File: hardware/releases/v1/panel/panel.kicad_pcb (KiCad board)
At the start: 4 copper layers, 55.6 x 77.4 mm, 83 parts, among them J1 KF142R-5.08-2P, J101 FPC-05F-8PH20, J102 OLED, J2 2086-1204/700-000/997-605, J3 FPC-05F-8PH20, J4 KF142R-5.08-3P, J5 2086-1203/700-000/997-605, J6 2086-1203/700-000/997-605, K1 G6B-2114P-US DC5, Q1 MMBT3904, SW101 B3U-1000P, SW102 B3U-1000P, U1 SCT2601TVBR, U101 74AHCT1G125, U2 LM66100, U3 XIAO ESP32C6

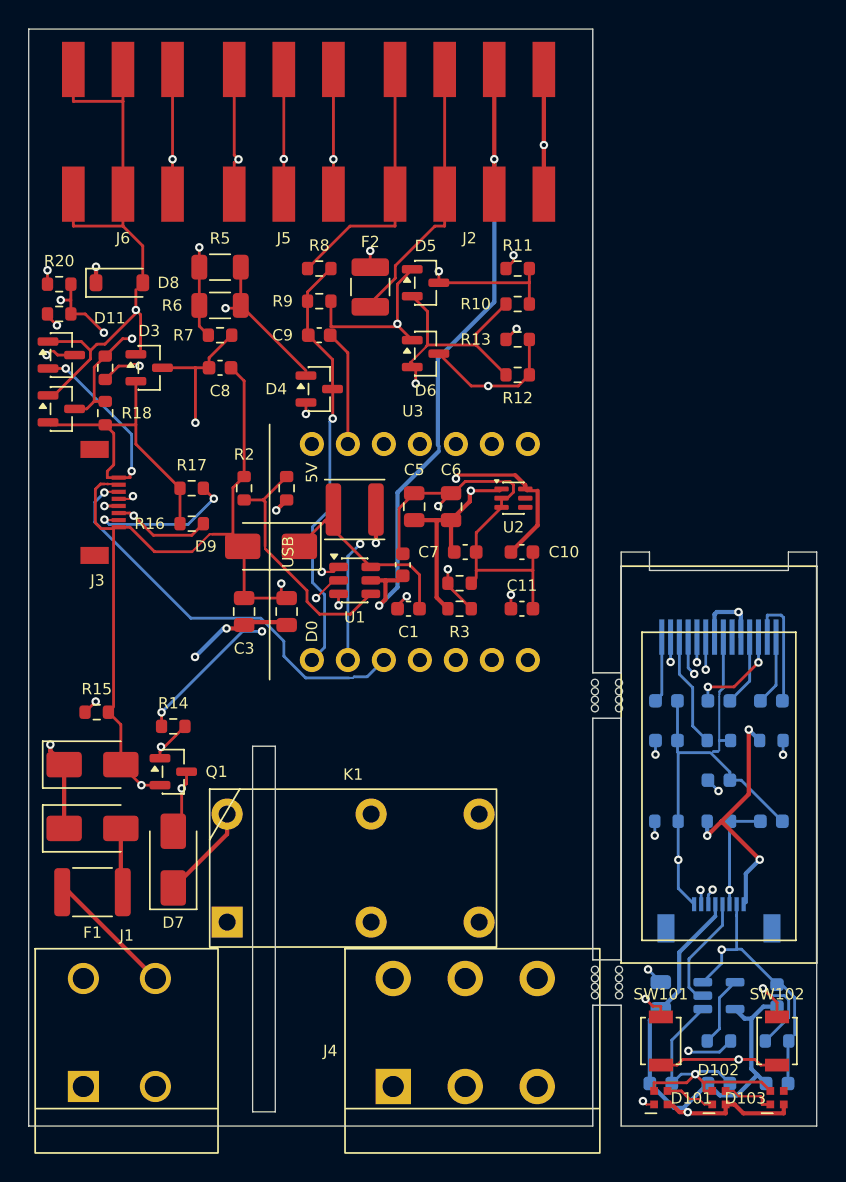
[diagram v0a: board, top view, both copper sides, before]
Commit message: extend GND track joints on main board to fully seat on pads/vias
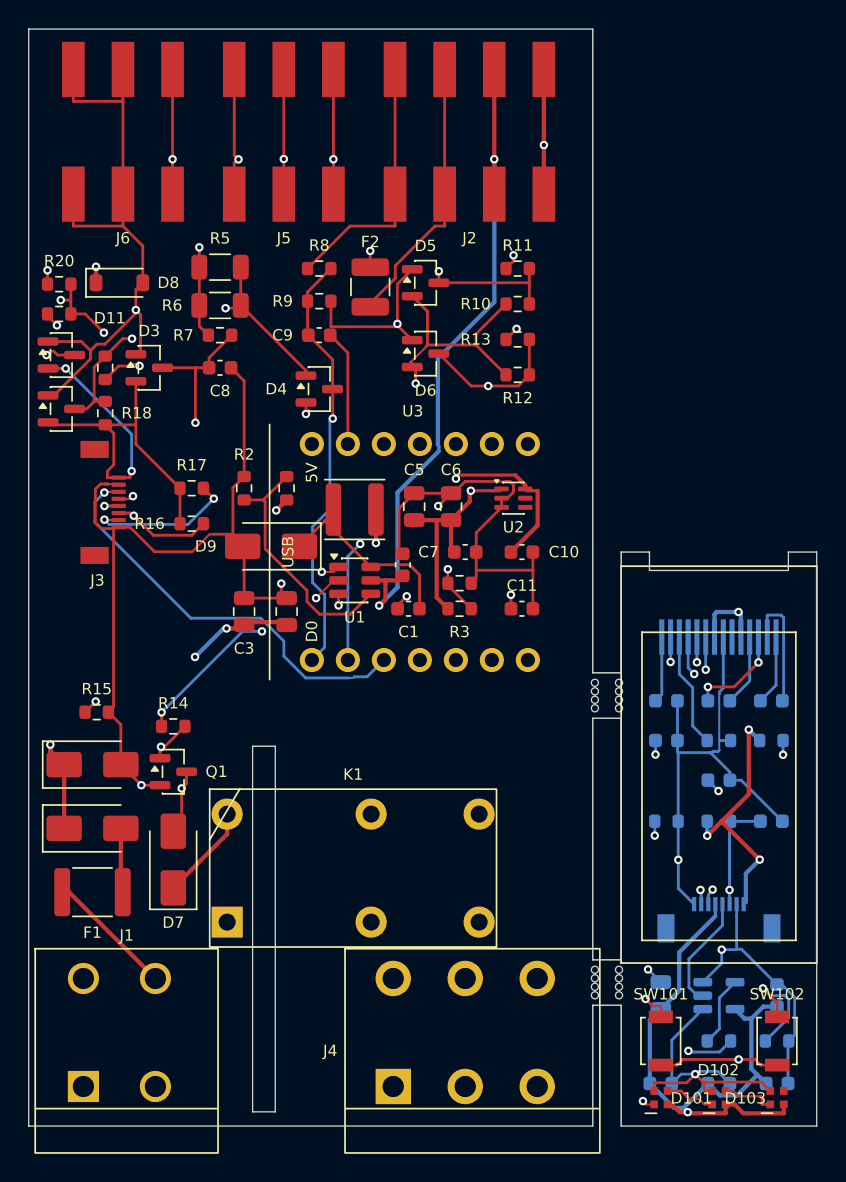
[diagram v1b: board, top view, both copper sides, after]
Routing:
- net GND: track 158.3 -> 160.1 mm
- net UI_GND: track 74.0 -> 75.4 mm
